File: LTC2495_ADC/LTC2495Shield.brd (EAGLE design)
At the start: 57.3 x 44.9 mm, 14 parts

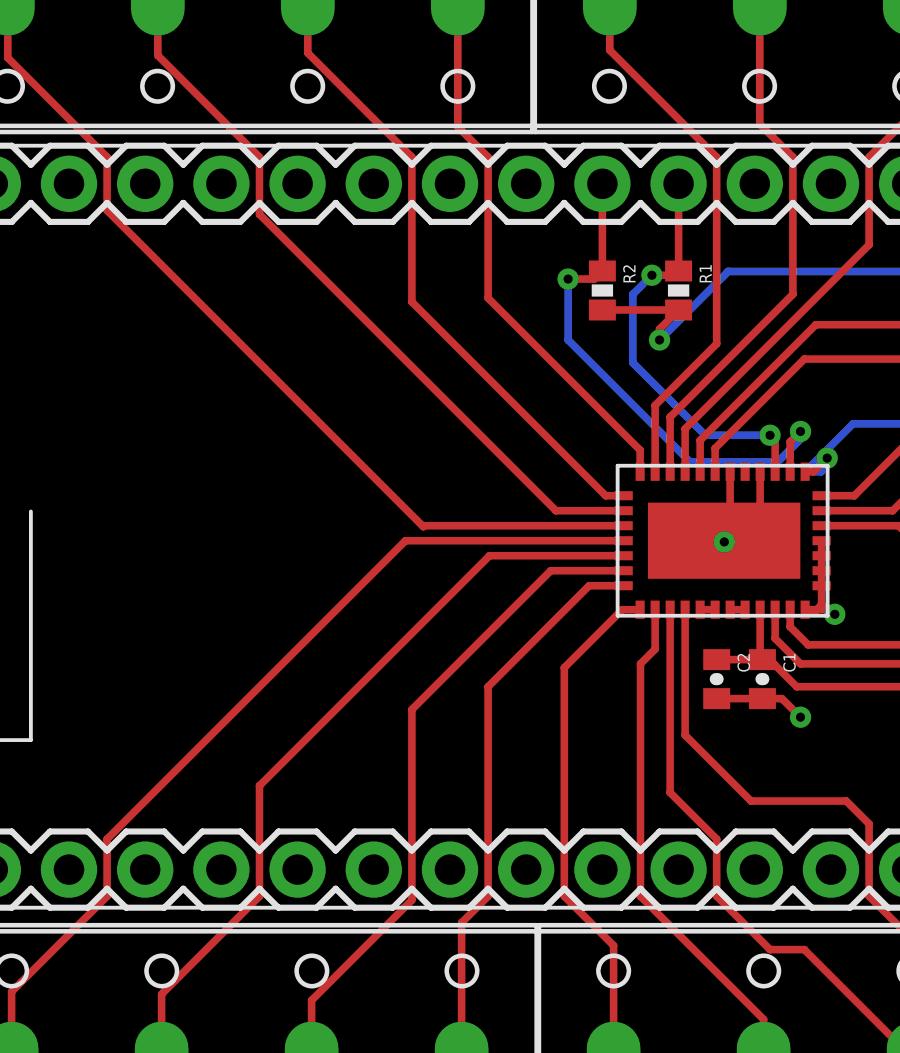
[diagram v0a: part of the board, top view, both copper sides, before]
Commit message: Updated the i2c pins to all shields to use d11/d12  as these pins will have dual use with the upcoming wifimcu Added FM24W256  Fram shield Added X95840 Digital potentiometer Shield Added AD5696 DAC Shield
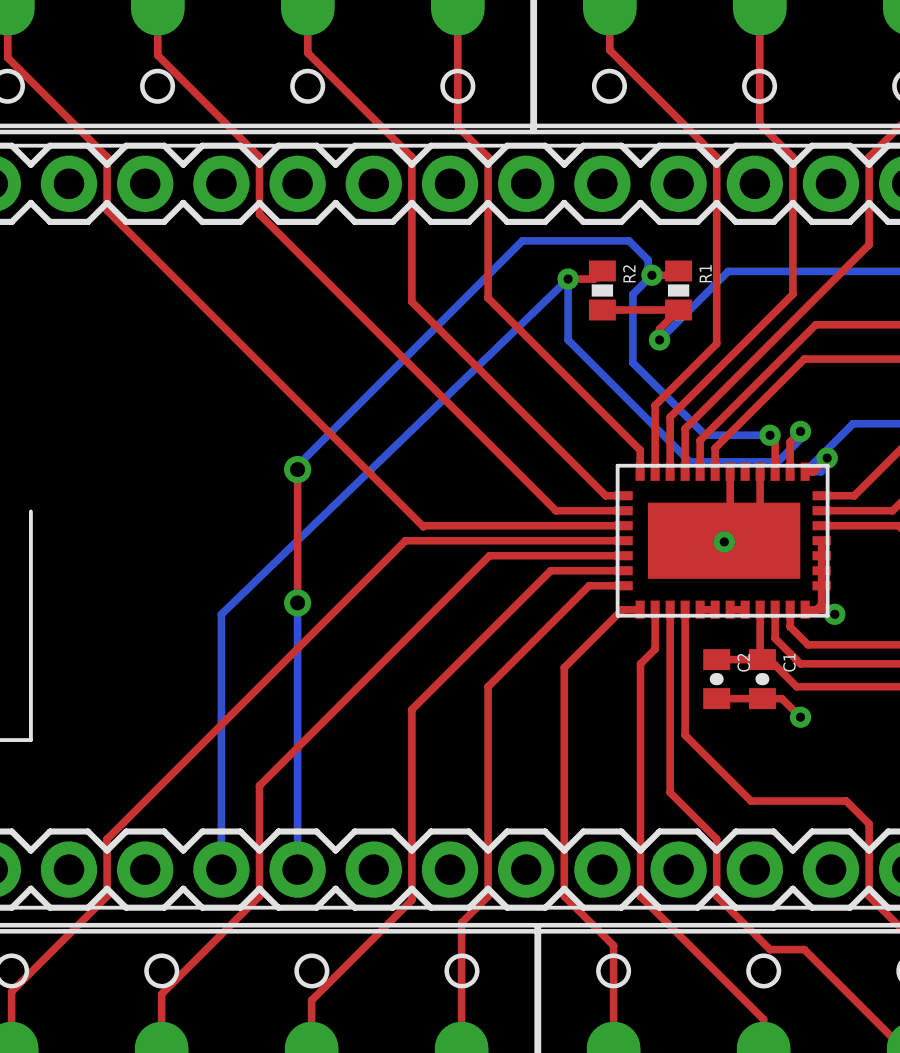
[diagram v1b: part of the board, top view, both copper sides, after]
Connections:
- net GND: no longer U$1.24
- net N$2: now also U$1.5; no longer U$1.21
- net N$8: now also U$1.4; no longer U$1.22
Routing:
- net N$2: track 13.9 -> 40.1 mm, vias 2 -> 4
- net N$8: track 17.8 -> 39.5 mm
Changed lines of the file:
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@@
 <contactref element="U$1" pad="10"/>
 <contactref element="U$1" pad="17"/>
-<contactref element="U$1" pad="24"/>
 </signal>
 <signal name="3.3V">
@@
 </signal>
 <signal name="N$2">
-<contactref element="U$1" pad="21"/>
 <contactref element="R1" pad="1"/>
-<wire x1="29.972" y1="34.29" x2="29.972" y2="31.384" width="0.254" layer="1"/>
 <contactref element="U$3" pad="P$3"/>
 <wire x1="33.19" y1="24.692" x2="33.19" y2="25.738" width="0.254" layer="1"/>
@@
 <wire x1="29.083" y1="31.242" x2="29.83" y2="31.242" width="0.254" layer="1"/>
 <wire x1="29.83" y1="31.242" x2="29.972" y2="31.384" width="0.254" layer="1"/>
+<contactref element="U$1" pad="5"/>
+<wire x1="17.272" y1="11.43" x2="17.272" y2="20.32" width="0.254" layer="16"/>
+<via x="17.272" y="20.32" extent="1-16" drill="0.5"/>
+<wire x1="17.272" y1="20.32" x2="17.272" y2="24.765" width="0.254" layer="1"/>
+<via x="17.272" y="24.765" extent="1-16" drill="0.5"/>
+<wire x1="17.272" y1="24.765" x2="17.272" y2="24.892" width="0.254" layer="16"/>
+<wire x1="17.272" y1="24.892" x2="24.765" y2="32.385" width="0.254" layer="16"/>
+<wire x1="24.765" y1="32.385" x2="28.321" y2="32.385" width="0.254" layer="16"/>
+<wire x1="28.321" y1="32.385" x2="28.956" y2="31.75" width="0.254" layer="16"/>
+<wire x1="28.956" y1="31.75" x2="28.956" y2="31.369" width="0.254" layer="16"/>
+<wire x1="28.956" y1="31.369" x2="29.083" y2="31.242" width="0.254" layer="16"/>
 </signal>
 <signal name="N$8">
-<contactref element="U$1" pad="22"/>
 <contactref element="R2" pad="1"/>
-<wire x1="27.432" y1="31.384" x2="27.432" y2="34.29" width="0.254" layer="1"/>
 <contactref element="U$3" pad="P$2"/>
 <wire x1="33.69" y1="24.692" x2="33.69" y2="25.689" width="0.254" layer="1"/>
@@
 <wire x1="26.289" y1="31.115" x2="27.163" y2="31.115" width="0.254" layer="1"/>
 <wire x1="27.163" y1="31.115" x2="27.432" y2="31.384" width="0.254" layer="1"/>
+<contactref element="U$1" pad="4"/>
+<wire x1="14.732" y1="11.43" x2="14.732" y2="19.939" width="0.254" layer="16"/>
+<wire x1="14.732" y1="19.939" x2="26.289" y2="31.115" width="0.254" layer="16"/>
 </signal>
 <signal name="N$3">
